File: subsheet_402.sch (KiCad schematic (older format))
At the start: 39 parts, among them J400 DIN-13S — Video Port, Q400 2N3904, Q401 2N3904, Q402 2N3904, Q403 2N3904, U405 74S257_PHY

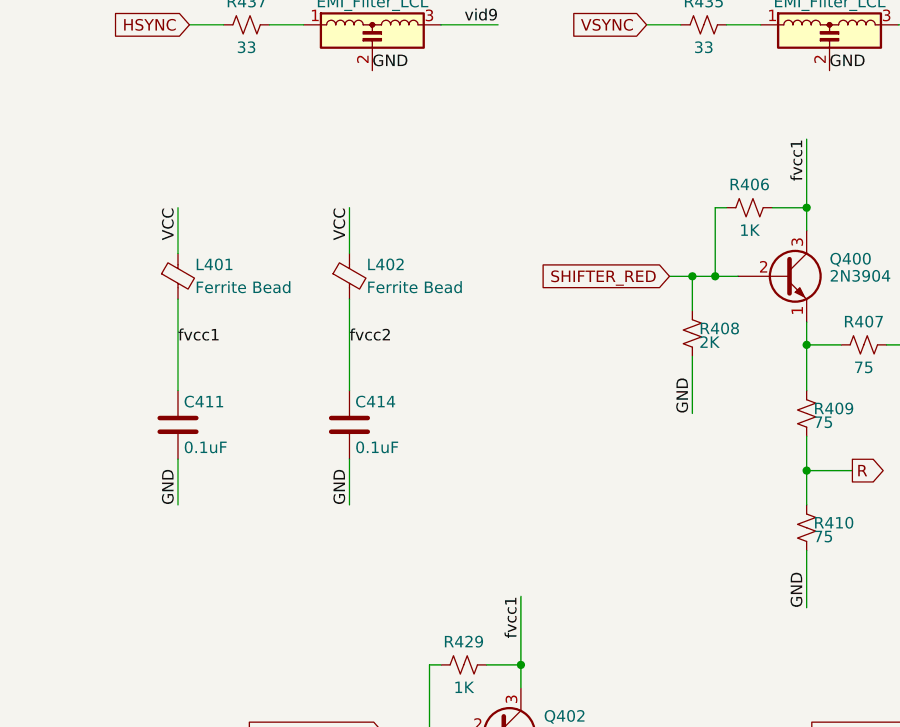
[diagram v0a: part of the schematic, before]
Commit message: [Schematics] Reference to the fix of video ghosting from Exxos
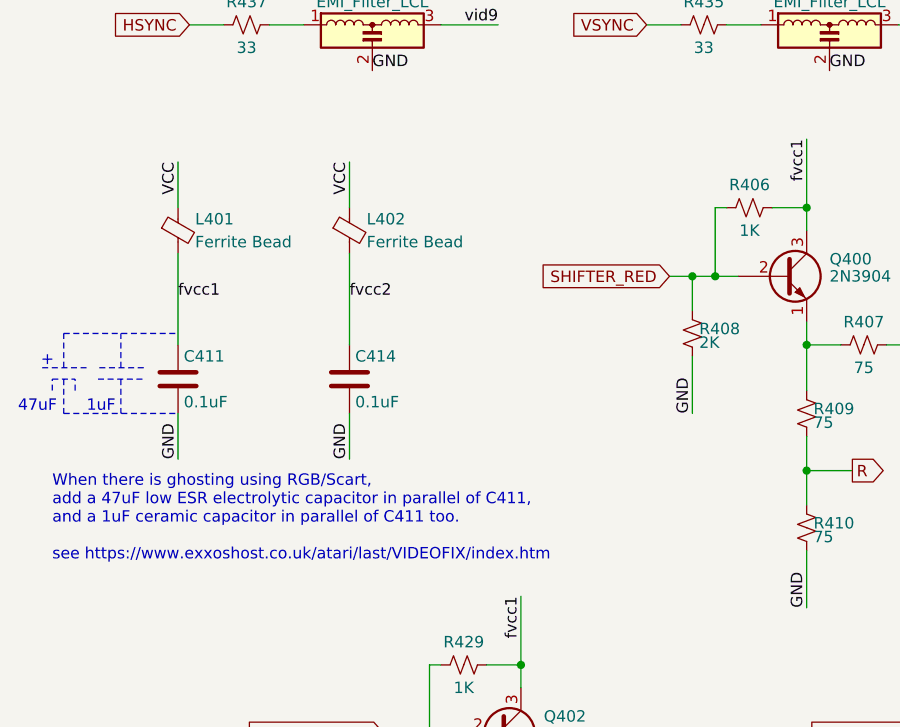
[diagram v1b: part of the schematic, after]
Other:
- note added: "+"
- note added: "1uF"
- note added: "47uF"
- note added: "When there is ghosting using RGB/Scart, \nadd a 47uF low ESR electrolytic capacitor in parallel of C411, \nand a 1uF ceramic capacitor in parallel of C411 too.\n\nsee https://www.exxoshost.co.uk/atari/last/VIDEOFIX/index.htm\n"
- moved on the sheet: C411, C414, L401, L402
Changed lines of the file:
@@
 L Device:Ferrite_Bead_Small L401
 U 1 1 60B41C5A
-P 1250 3700
-F 0 "L401" H 1325 3750 50  0000 L CNN
-F 1 "Ferrite Bead" H 1325 3650 50  0000 L CNN
-F 2 "commons_passives_THT:Passive_THT_ferrite_bead_W3.81mm_L15.24mm" V 1180 3700 50  0001 C CNN
-F 3 "~" H 1250 3700 50  0001 C CNN
-	1    1250 3700
+P 1250 3500
+F 0 "L401" H 1325 3550 50  0000 L CNN
+F 1 "Ferrite Bead" H 1325 3450 50  0000 L CNN
+F 2 "commons_passives_THT:Passive_THT_ferrite_bead_W3.81mm_L15.24mm" V 1180 3500 50  0001 C CNN
+F 3 "~" H 1250 3500 50  0001 C CNN
+	1    1250 3500
 	1    0    0    -1
 $EndComp
@@
 L Device:C C?
 U 1 1 60B4784B
-P 1250 4350
+P 1250 4150
 AR Path="/60786F27/6078774E/60B4784B" Ref="C?"  Part="1"
 AR Path="/60786F27/607875AF/60B4784B" Ref="C?"  Part="1"
@@
 AR Path="/60AD33B6/60B4784B" Ref="C?"  Part="1"
 AR Path="/60B3D9E3/60B4784B" Ref="C411"  Part="1"
-F 0 "C411" H 1275 4450 50  0000 L CNN
-F 1 "0.1uF" H 1275 4250 50  0000 L CNN
-F 2 "commons_passives_THT:Passive_THT_capacitor_mlcc_W2.54mm_L10.16mm" H 1288 4200 50  0001 C CNN
-F 3 "~" H 1250 4350 50  0001 C CNN
-	1    1250 4350
-	1    0    0    -1
-$EndComp
-Text Label 1250 4700 1    50   ~ 0
-GND
-Wire Wire Line
-	1250 4500 1250 4700
-Text Label 1250 4000 0    50   ~ 0
+F 0 "C411" H 1275 4250 50  0000 L CNN
+F 1 "0.1uF" H 1275 4050 50  0000 L CNN
+F 2 "commons_passives_THT:Passive_THT_capacitor_mlcc_W2.54mm_L10.16mm" H 1288 4000 50  0001 C CNN
+F 3 "~" H 1250 4150 50  0001 C CNN
+	1    1250 4150
+	1    0    0    -1
+$EndComp
+Text Label 1250 4500 1    50   ~ 0
+GND
+Wire Wire Line
+	1250 4300 1250 4500
+Text Label 1250 3800 0    50   ~ 0
 fvcc1
 Wire Wire Line
-	1250 3600 1250 3400
-Text Label 1250 3400 3    50   ~ 0
+	1250 3400 1250 3200
+Text Label 1250 3200 3    50   ~ 0
 VCC
 $Comp
 L Device:Ferrite_Bead_Small L402
 U 1 1 60B49A84
-P 2000 3700
-F 0 "L402" H 2075 3750 50  0000 L CNN
-F 1 "Ferrite Bead" H 2075 3650 50  0000 L CNN
-F 2 "commons_passives_THT:Passive_THT_ferrite_bead_W3.81mm_L15.24mm" V 1930 3700 50  0001 C CNN
-F 3 "~" H 2000 3700 50  0001 C CNN
-	1    2000 3700
+P 2000 3500
+F 0 "L402" H 2075 3550 50  0000 L CNN
+F 1 "Ferrite Bead" H 2075 3450 50  0000 L CNN
+F 2 "commons_passives_THT:Passive_THT_ferrite_bead_W3.81mm_L15.24mm" V 1930 3500 50  0001 C CNN
+F 3 "~" H 2000 3500 50  0001 C CNN
+	1    2000 3500
 	1    0    0    -1
 $EndComp
@@
 L Device:C C?
 U 1 1 60B49A8A
-P 2000 4350
+P 2000 4150
 AR Path="/60786F27/6078774E/60B49A8A" Ref="C?"  Part="1"
 AR Path="/60786F27/607875AF/60B49A8A" Ref="C?"  Part="1"
@@
 AR Path="/60AD33B6/60B49A8A" Ref="C?"  Part="1"
 AR Path="/60B3D9E3/60B49A8A" Ref="C414"  Part="1"
-F 0 "C414" H 2025 4450 50  0000 L CNN
-F 1 "0.1uF" H 2025 4250 50  0000 L CNN
-F 2 "commons_passives_THT:Passive_THT_capacitor_mlcc_W2.54mm_L7.62mm" H 2038 4200 50  0001 C CNN
-F 3 "~" H 2000 4350 50  0001 C CNN
-	1    2000 4350
-	1    0    0    -1
-$EndComp
-Text Label 2000 4700 1    50   ~ 0
-GND
-Wire Wire Line
-	2000 4500 2000 4700
-Text Label 2000 4000 0    50   ~ 0
+F 0 "C414" H 2025 4250 50  0000 L CNN
+F 1 "0.1uF" H 2025 4050 50  0000 L CNN
+F 2 "commons_passives_THT:Passive_THT_capacitor_mlcc_W2.54mm_L7.62mm" H 2038 4000 50  0001 C CNN
+F 3 "~" H 2000 4150 50  0001 C CNN
+	1    2000 4150
+	1    0    0    -1
+$EndComp
+Text Label 2000 4500 1    50   ~ 0
+GND
+Wire Wire Line
+	2000 4300 2000 4500
+Text Label 2000 3800 0    50   ~ 0
 fvcc2
 Wire Wire Line
-	2000 3600 2000 3400
-Text Label 2000 3400 3    50   ~ 0
+	2000 3400 2000 3200
+Text Label 2000 3200 3    50   ~ 0
 VCC
 Wire Wire Line
-	1250 3800 1250 4200
-Wire Wire Line
-	2000 3800 2000 4200
+	1250 3600 1250 4000
+Wire Wire Line
+	2000 3600 2000 4000
 $Comp
 L Transistor_BJT:2N3904 Q400
@@
 Wire Wire Line
 	6350 2900 6350 2700
+Text Notes 700  4950 0    50   ~ 0
+When there is ghosting using RGB/Scart, \nadd a 47uF low ESR electrolytic capacitor in parallel of C411, \nand a 1uF ceramic capacitor in parallel of C411 too.\n\nsee https://www.exxoshost.co.uk/atari/last/VIDEOFIX/index.htm\n
+Wire Notes Line
+	1100 4100 900  4100
+Wire Notes Line
+	900  4150 1100 4150
+Wire Notes Line
+	850  4100 650  4100
+Wire Notes Line
+	750  4150 750  4300
+Wire Notes Line
+	750  4300 1250 4300
+Wire Notes Line
+	1000 4150 1000 4300
+Wire Notes Line
+	750  4100 750  3950
+Wire Notes Line
+	750  3950 1250 3950
+Wire Notes Line
+	1000 4100 1000 3950
+Wire Notes Line
+	700  4200 700  4150
+Wire Notes Line
+	800  4200 800  4150
+Wire Notes Line
+	700  4150 800  4150
+Text Notes 550  4300 0    50   ~ 0
+47uF
+Text Notes 650  4100 0    50   ~ 0
++
+Text Notes 850  4300 0    50   ~ 0
+1uF
 $EndSCHEMATC
